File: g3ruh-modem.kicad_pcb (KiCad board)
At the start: 2 copper layers, 160 x 100 mm, 110 parts, among them P1 CONN_01X03, P2 CONN_01X06, P3 CONN_01X05, P4 C96ABC, Q1 LM7805_TO220, U1 4029, U10 LM339, U11 74HC14, U12 74HC164, U13 74HC86, U14 74HC164, U15 27C128, U16 TL084, U17 74HC74, U18 74HC164, U19 ZN429E-8, U2 27C128, U3 4029, U4 74HC164, U5 74HC74, U6 74HC86, U7 74HC164, U8 74HC161, U9 ZN429E-8

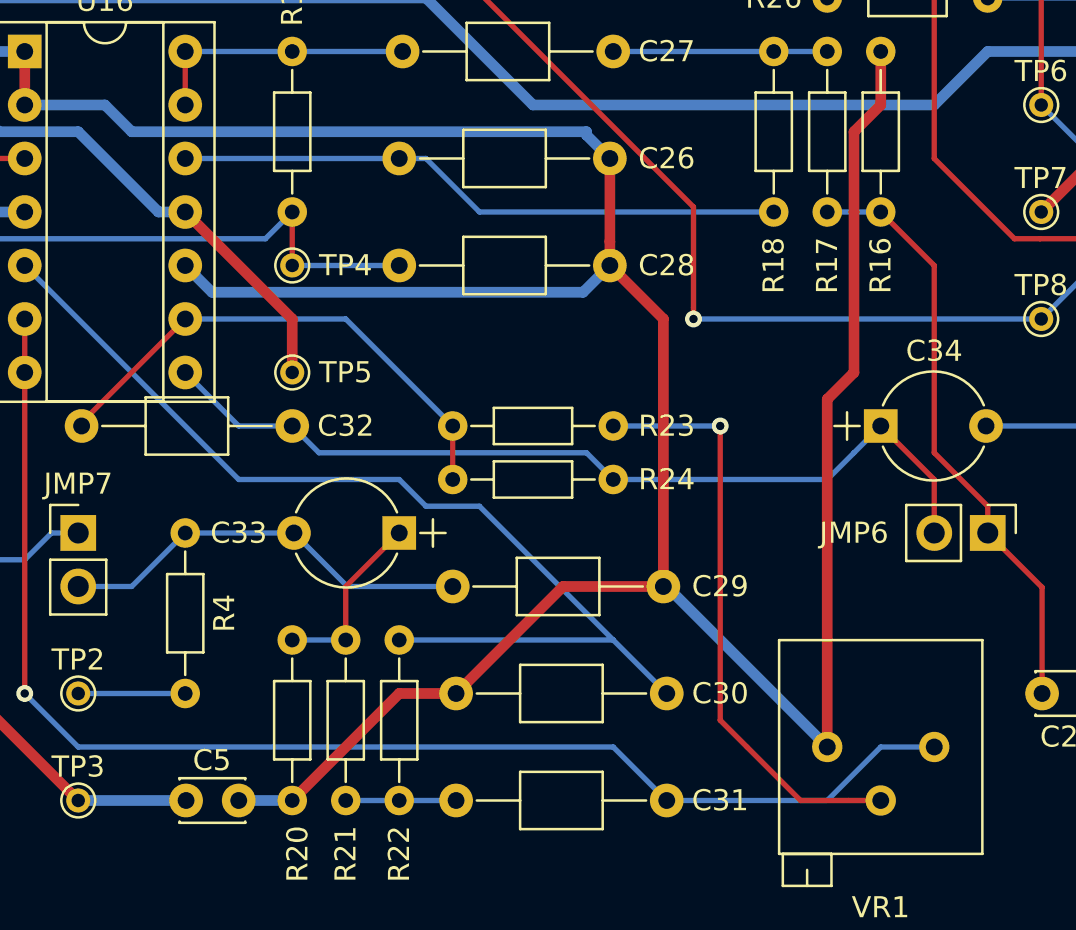
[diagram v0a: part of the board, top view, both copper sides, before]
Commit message: Added extra pads for pot VR1 to allow for a variety of possible parts.
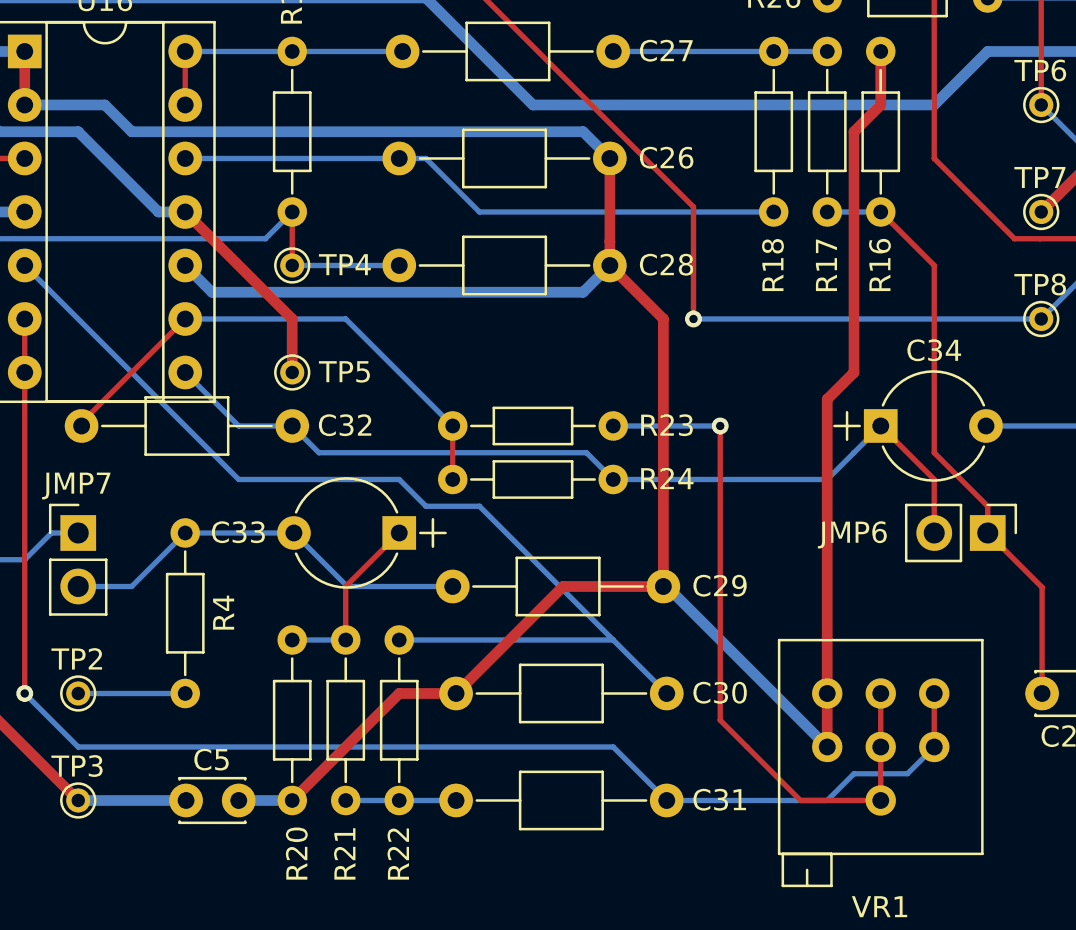
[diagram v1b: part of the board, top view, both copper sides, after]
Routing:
- net Net-(R23-Pad1): track 28.2 -> 33.3 mm
- net Net-(C31-Pad1): track 64.1 -> 66.7 mm

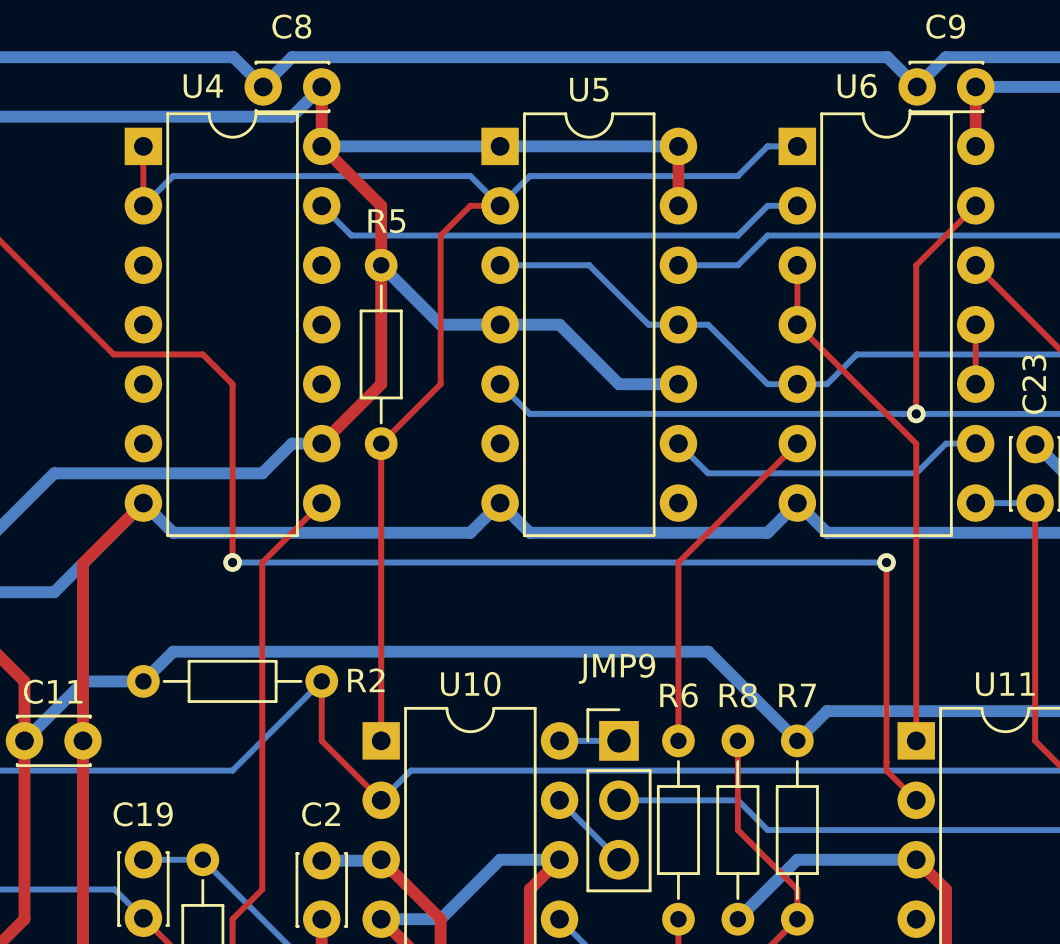
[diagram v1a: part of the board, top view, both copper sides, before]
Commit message: Corrected transcription errors.
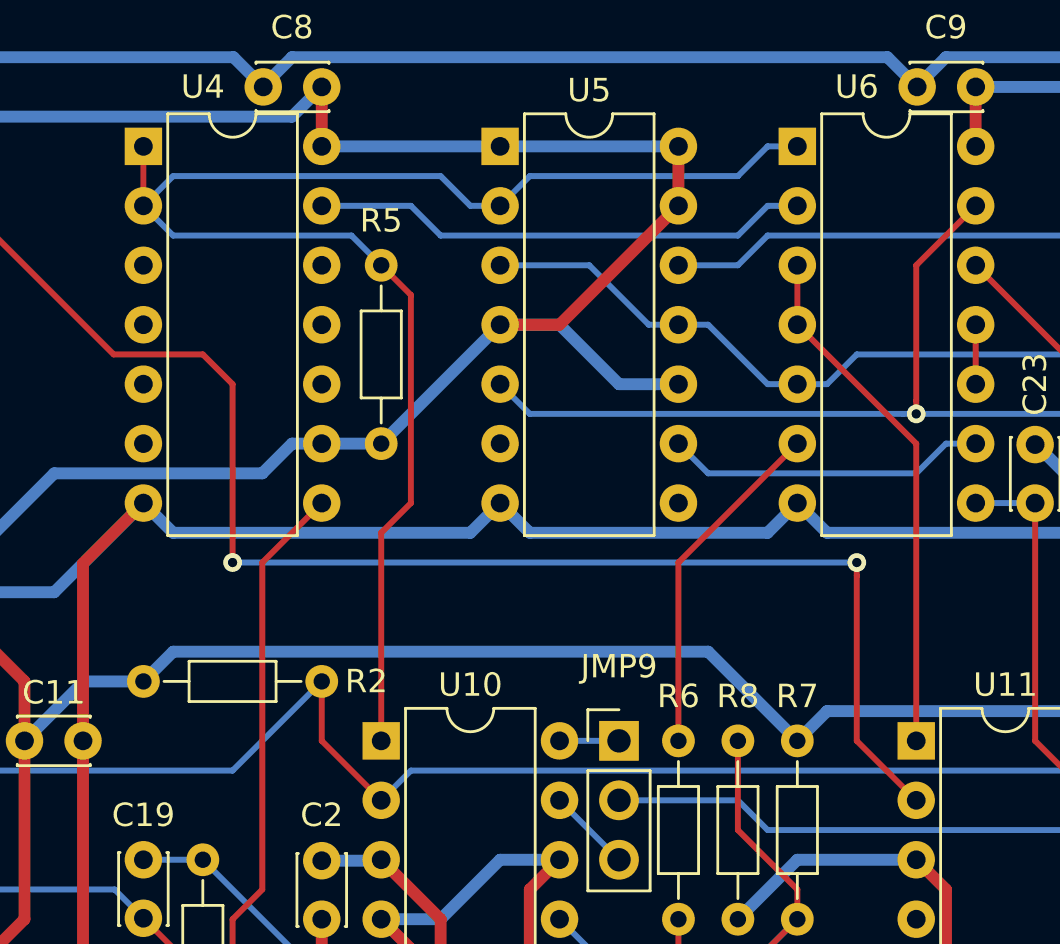
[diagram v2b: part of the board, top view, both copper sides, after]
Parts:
- R2: value 47K -> 4K7
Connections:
- R5 pad 1: /UNSCRAMBLER/RX_FILTER -> +5V
- R5 pad 2: +5V -> /UNSCRAMBLER/RX_FILTER
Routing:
- net /UNSCRAMBLER/RX_FILTER: track 58.3 -> 65.2 mm
- net +5V: track 575.9 -> 574.4 mm
- net Net-(U1-Pad15): track 97.4 -> 96.7 mm
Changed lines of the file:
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@@
 (kicad_pcb (version 4) (host pcbnew 4.0.7)
   (general
-    (links 330)
+    (links 334)
     (no_connects 0)
-    (area 73.074999 43.294999 233.225001 143.445001)
+    (area 68.621429 43.294999 237.522401 143.445001)
     (thickness 1.6)
     (drawings 4)
-    (tracks 952)
+    (tracks 954)
     (zones 0)
     (modules 110)
@@
   )
   (setup
-    (last_trace_width 0.508)
+    (last_trace_width 0.25)
     (user_trace_width 0.254)
     (user_trace_width 0.508)
@@
     (aux_axis_origin 0 0)
     (grid_origin 229.55 137.77)
-    (visible_elements FFFFF729)
+    (visible_elements FFFFFF29)
     (pcbplotparams
       (layerselection 0x00030_ffffffff)
@@
       (effects (font (size 1 1) (thickness 0.15)))
     )
-    (fp_text value 47K (at 3.81 0) (layer F.Fab)
+    (fp_text value 4K7 (at 3.81 0) (layer F.Fab)
       (effects (font (size 1 1) (thickness 0.15)))
     )
@@
     (descr "Resistor, Axial_DIN0204 series, Axial, Horizontal, pin pitch=7.62mm, 0.16666666666666666W = 1/6W, length*diameter=3.6*1.6mm^2, http://cdn-reichelt.de/documents/datenblatt/B400/1_4W%23YAG.pdf")
     (tags "Resistor Axial_DIN0204 series Axial Horizontal pin pitch 7.62mm 0.16666666666666666W = 1/6W length 3.6mm diameter 1.6mm")
-    (fp_text reference R5 (at 9.475 0.235 180) (layer F.SilkS)
+    (fp_text reference R5 (at 9.525 0 180) (layer F.SilkS)
       (effects (font (size 1 1) (thickness 0.15)))
     )
@@
     (fp_line (start 8.6 -1.15) (end -0.95 -1.15) (layer F.CrtYd) (width 0.05))
     (pad 1 thru_hole circle (at 0 0 90) (size 1.4 1.4) (drill 0.7) (layers *.Cu *.Mask)
-      (net 230 /UNSCRAMBLER/RX_FILTER))
-    (pad 2 thru_hole oval (at 7.62 0 90) (size 1.4 1.4) (drill 0.7) (layers *.Cu *.Mask)
       (net 2 +5V))
+    (pad 2 thru_hole oval (at 7.62 0 90) (size 1.4 1.4) (drill 0.7) (layers *.Cu *.Mask)
+      (net 230 /UNSCRAMBLER/RX_FILTER))
     (model Resistors_THT.3dshapes/R_Axial_DIN0204_L3.6mm_D1.6mm_P7.62mm_Horizontal.wrl
       (at (xyz 0 0 0))
@@
   (segment (start 148.27 81.93) (end 150.77 81.93) (width 0.508) (layer B.Cu) (net 1))
   (segment (start 150.77 81.93) (end 150.81 81.89) (width 0.508) (layer B.Cu) (net 1))
+  (segment (start 155.89 59.03) (end 158.43 59.03) (width 0.508) (layer F.Cu) (net 2))
+  (segment (start 158.43 59.03) (end 163.51 53.95) (width 0.508) (layer F.Cu) (net 2))
+  (segment (start 155.89 59.03) (end 150.81 64.11) (width 0.508) (layer B.Cu) (net 2))
+  (segment (start 148.27 64.11) (end 150.81 64.11) (width 0.508) (layer B.Cu) (net 2))
   (segment (start 96.2 52.68) (end 97.47 51.41) (width 0.508) (layer F.Cu) (net 2))
   (segment (start 94.93 53.95) (end 96.2 52.68) (width 0.508) (layer F.Cu) (net 2))
@@
   (segment (start 158.43 59.03) (end 155.89 59.03) (width 0.508) (layer B.Cu) (net 2))
   (segment (start 160.97 61.57) (end 158.43 59.03) (width 0.508) (layer B.Cu) (net 2))
-  (segment (start 155.89 59.03) (end 153.35 59.03) (width 0.508) (layer B.Cu) (net 2))
-  (segment (start 153.35 59.03) (end 150.81 56.49) (width 0.508) (layer B.Cu) (net 2))
-  (segment (start 150.81 56.49) (end 150.81 61.57) (width 0.508) (layer F.Cu) (net 2))
-  (segment (start 150.81 61.57) (end 148.27 64.11) (width 0.508) (layer F.Cu) (net 2))
-  (segment (start 148.27 51.41) (end 150.81 53.95) (width 0.508) (layer F.Cu) (net 2))
-  (segment (start 150.81 53.95) (end 150.81 56.49) (width 0.508) (layer F.Cu) (net 2))
   (segment (start 148.27 51.41) (end 148.27 48.87) (width 0.508) (layer F.Cu) (net 2))
   (segment (start 155.89 51.41) (end 148.27 51.41) (width 0.508) (layer B.Cu) (net 2))
@@
   (segment (start 89.85 66.65) (end 91.12 66.65) (width 0.254) (layer B.Cu) (net 147))
   (segment (start 125.41 61.57) (end 121.6 65.38) (width 0.254) (layer F.Cu) (net 147))
+  (segment (start 171.13 76.81) (end 171.13 69.755685) (width 0.254) (layer F.Cu) (net 148))
+  (segment (start 173.67 79.35) (end 171.13 76.81) (width 0.254) (layer F.Cu) (net 148))
+  (segment (start 171.13 69.755685) (end 171.13 69.19) (width 0.254) (layer F.Cu) (net 148))
+  (via (at 171.13 69.19) (size 0.8) (drill 0.4) (layers F.Cu B.Cu) (net 148))
+  (segment (start 144.46 69.19) (end 171.13 69.19) (width 0.254) (layer B.Cu) (net 148))
   (segment (start 143.19 60.3) (end 139.38 60.3) (width 0.254) (layer F.Cu) (net 148))
   (segment (start 144.46 61.57) (end 143.19 60.3) (width 0.254) (layer F.Cu) (net 148))
   (segment (start 144.46 69.19) (end 144.46 61.57) (width 0.254) (layer F.Cu) (net 148))
-  (segment (start 172.4 69.19) (end 144.46 69.19) (width 0.254) (layer B.Cu) (net 148))
   (segment (start 133.03 53.95) (end 139.38 60.3) (width 0.254) (layer F.Cu) (net 148))
   (via (at 144.46 69.19) (size 0.8) (drill 0.4) (layers F.Cu B.Cu) (net 148))
-  (segment (start 173.67 79.35) (end 172.4 78.08) (width 0.254) (layer F.Cu) (net 148))
-  (segment (start 172.4 78.08) (end 172.4 77.728602) (width 0.254) (layer F.Cu) (net 148))
-  (segment (start 172.4 77.728602) (end 172.4 69.19) (width 0.254) (layer F.Cu) (net 148))
-  (via (at 172.4 69.19) (size 0.8) (drill 0.4) (layers F.Cu B.Cu) (net 148))
   (segment (start 131.76 52.68) (end 98.74 52.68) (width 0.254) (layer B.Cu) (net 148))
   (segment (start 98.74 52.68) (end 97.47 53.95) (width 0.254) (layer B.Cu) (net 148))
@@
   (segment (start 102.55 81.89) (end 104.895962 81.89) (width 0.254) (layer B.Cu) (net 163))
   (segment (start 104.895962 81.89) (end 111.245962 88.24) (width 0.254) (layer B.Cu) (net 163))
-  (segment (start 166.05 55.22) (end 149.54 55.22) (width 0.254) (layer B.Cu) (net 166))
-  (segment (start 149.54 55.22) (end 148.27 53.95) (width 0.254) (layer B.Cu) (net 166))
-  (segment (start 167.32 53.95) (end 166.05 55.22) (width 0.254) (layer B.Cu) (net 166))
-  (segment (start 168.59 53.95) (end 167.32 53.95) (width 0.254) (layer B.Cu) (net 166))
+  (segment (start 166.05 55.22) (end 153.35 55.22) (width 0.254) (layer B.Cu) (net 166))
+  (segment (start 152.08 53.95) (end 153.35 55.22) (width 0.254) (layer B.Cu) (net 166))
+  (segment (start 148.27 53.95) (end 152.08 53.95) (width 0.254) (layer B.Cu) (net 166))
+  (segment (start 166.05 55.22) (end 167.32 53.95) (width 0.254) (layer B.Cu) (net 166))
+  (segment (start 167.32 53.95) (end 168.59 53.95) (width 0.254) (layer B.Cu) (net 166))
   (segment (start 191.45 53.95) (end 190.18 55.22) (width 0.254) (layer B.Cu) (net 175))
   (segment (start 190.18 55.22) (end 167.32 55.22) (width 0.254) (layer B.Cu) (net 175))
@@
   (segment (start 181.29 125.07) (end 176.21 125.07) (width 0.25) (layer B.Cu) (net 228))
   (segment (start 209.23 81.89) (end 216.85 81.89) (width 0.508) (layer B.Cu) (net 229))
-  (segment (start 150.81 64.11) (end 150.81 76.81) (width 0.254) (layer F.Cu) (net 230))
-  (segment (start 154.62 53.95) (end 155.89 53.95) (width 0.254) (layer F.Cu) (net 230))
-  (segment (start 153.35 55.22) (end 154.62 53.95) (width 0.254) (layer F.Cu) (net 230))
-  (segment (start 153.35 61.57) (end 153.35 55.22) (width 0.254) (layer F.Cu) (net 230))
-  (segment (start 150.81 64.11) (end 153.35 61.57) (width 0.254) (layer F.Cu) (net 230))
+  (segment (start 154.62 53.95) (end 155.89 53.95) (width 0.254) (layer B.Cu) (net 230))
+  (segment (start 153.35 52.68) (end 154.62 53.95) (width 0.254) (layer B.Cu) (net 230))
+  (segment (start 141.92 52.68) (end 153.35 52.68) (width 0.254) (layer B.Cu) (net 230))
+  (segment (start 140.65 53.95) (end 141.92 52.68) (width 0.254) (layer B.Cu) (net 230))
+  (segment (start 149.54 55.22) (end 141.92 55.22) (width 0.254) (layer B.Cu) (net 230))
+  (segment (start 141.92 55.22) (end 140.65 53.95) (width 0.254) (layer B.Cu) (net 230))
+  (segment (start 150.81 56.49) (end 149.54 55.22) (width 0.254) (layer B.Cu) (net 230))
+  (segment (start 150.81 67.92) (end 150.81 76.81) (width 0.254) (layer F.Cu) (net 230))
+  (segment (start 152.08 66.65) (end 150.81 67.92) (width 0.254) (layer F.Cu) (net 230))
+  (segment (start 152.08 57.76) (end 152.08 66.65) (width 0.254) (layer F.Cu) (net 230))
+  (segment (start 150.81 56.49) (end 152.08 57.76) (width 0.254) (layer F.Cu) (net 230))
   (segment (start 166.05 52.68) (end 167.32 51.41) (width 0.254) (layer B.Cu) (net 230))
   (segment (start 167.32 51.41) (end 168.59 51.41) (width 0.254) (layer B.Cu) (net 230))
   (segment (start 157.16 52.68) (end 166.05 52.68) (width 0.254) (layer B.Cu) (net 230))
   (segment (start 155.89 53.95) (end 157.16 52.68) (width 0.254) (layer B.Cu) (net 230))
-  (segment (start 154.62 52.68) (end 155.89 53.95) (width 0.254) (layer B.Cu) (net 230))
-  (segment (start 141.92 52.68) (end 154.62 52.68) (width 0.254) (layer B.Cu) (net 230))
-  (segment (start 140.65 53.95) (end 141.92 52.68) (width 0.254) (layer B.Cu) (net 230))
   (segment (start 140.65 53.95) (end 140.65 51.41) (width 0.254) (layer F.Cu) (net 230))
   (segment (start 92.39 94.59) (end 92.39 79.35) (width 0.254) (layer F.Cu) (net 231))
